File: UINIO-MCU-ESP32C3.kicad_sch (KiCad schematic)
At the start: 1 part

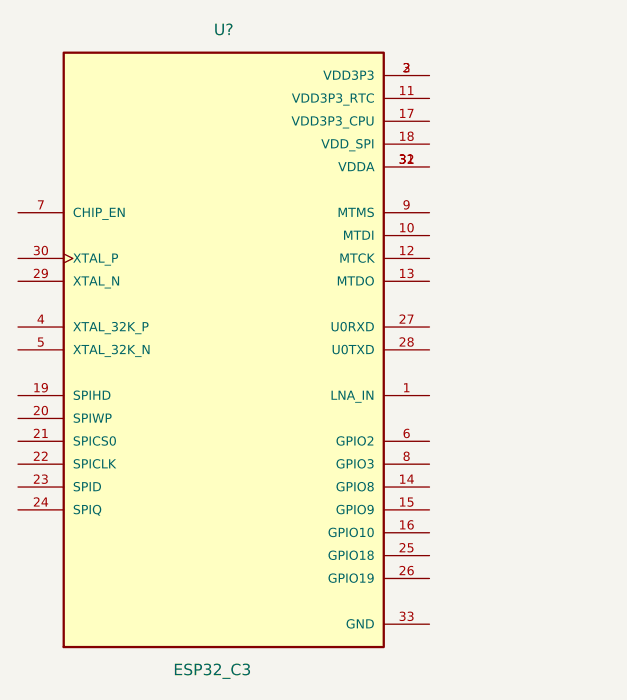
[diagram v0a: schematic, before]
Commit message: Replace ESP32-C3 Symbol.
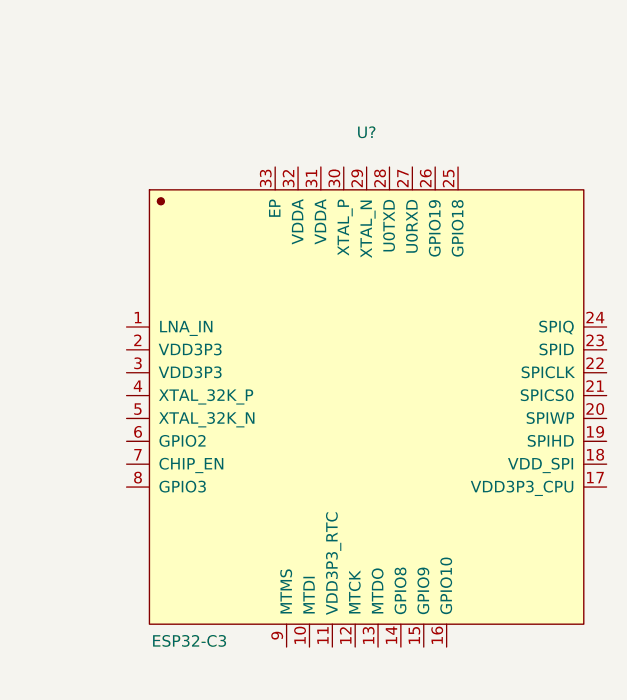
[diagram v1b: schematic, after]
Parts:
- removed U?: ESP32_C3, Uinio:QFN-32-5-5, symbol Uinio:ESP32_C3
- added U?: ESP32-C3, kicad_lceda:QFN-32_L5.0-W5.0-P0.50-TL-EP3.7, symbol Uinio:ESP32-C3
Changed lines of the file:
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@@
     (company "电子技术博客 UinIO.com")
   )
-  (symbol (lib_id "Uinio:ESP32_C3") (at 143.51 90.17 0) (unit 1)
+  (symbol (lib_id "Uinio:ESP32-C3") (at 154.305 96.52 0) (unit 1)
     (in_bom yes) (on_board yes)
-    (property "Reference" "U?" (id 0) (at 143.51 54.61 0))
-    (property "Value" "ESP32_C3" (id 1) (at 142.24 125.73 0))
-    (property "Footprint" "Uinio:QFN-32-5-5" (id 2) (at 132.08 127 0)
-      (effects (font (size 1.27 1.27)) (justify left bottom) hide)
+    (property "Reference" "U?" (id 0) (at 159.385 66.04 0))
+    (property "Value" "ESP32-C3" (id 1) (at 139.7 122.555 0))
+    (property "Footprint" "kicad_lceda:QFN-32_L5.0-W5.0-P0.50-TL-EP3.7" (id 2) (at 159.385 134.62 0)
+      (effects (font (size 1.27 1.27)) hide)
     )
-    (property "Datasheet" "" (id 3) (at 143.51 90.17 0)
-      (effects (font (size 1.27 1.27)) (justify left bottom) hide)
+    (property "Datasheet" "" (id 3) (at 154.305 76.8604 0)
+      (effects (font (size 1.27 1.27)) hide)
     )
-    (property "STANDARD" "" (id 4) (at 166.37 52.07 0)
-      (effects (font (size 1.27 1.27)) (justify left bottom) hide)
+    (property "SuppliersPartNumber" "C2838500" (id 4) (at 154.305 81.9404 0)
+      (effects (font (size 1.27 1.27)) hide)
     )
-    (property "MANUFACTURER" "" (id 5) (at 139.7 52.07 0)
-      (effects (font (size 1.27 1.27)) (justify left bottom) hide)
-    )
-    (property "PARTREV" "" (id 6) (at 163.83 49.53 0)
-      (effects (font (size 1.27 1.27)) (justify left bottom) hide)
-    )
-    (property "MAXIMUM_PACKAGE_HEIGHT" "" (id 7) (at 156.21 49.53 0)
-      (effects (font (size 1.27 1.27)) (justify left bottom) hide)
+    (property "uuid" "std:eaf37c2b292749de92559c0e914f3f30" (id 5) (at 160.655 138.43 0)
+      (effects (font (size 1.27 1.27)) hide)
     )
     (pin "1")
@@
   )
   (symbol_instances
-    (path "/826bd899-525d-4541-8e56-7c1d58c325f6"
-      (reference "U?") (unit 1) (value "ESP32_C3") (footprint "Uinio:QFN-32-5-5")
+    (path "/6af47f04-0cf9-428d-a0f2-32519eb3eeb0"
+      (reference "U?") (unit 1) (value "ESP32-C3") (footprint "kicad_lceda:QFN-32_L5.0-W5.0-P0.50-TL-EP3.7")
     )
   )

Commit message: update
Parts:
- added AE?: Antenna, symbol Device:Antenna
- added C? (x7): 0.1uF, symbol Device:C
- added C? (x2): 0.1uF, Capacitor_SMD:C_0603_1608Metric, symbol Device:C
- added C?: 1uF, Capacitor_SMD:C_0603_1608Metric, symbol Device:C
- added C? (x2): 15pF, symbol Device:C
- added C? (x2): 1uF, Capacitor_SMD:C_0402_1005Metric, symbol Uinio:CAP_0402
- added C? (x2): 1uF, symbol Device:C
- added C?: 10nF, symbol Device:C
- added D? (x2): BLUE LED, LED_SMD:LED_0603_1608Metric, symbol Device:LED
- added D?: Green LED, LED_SMD:LED_0603_1608Metric, symbol Device:LED
- added F?: Polyfuse, Fuse:Fuse_1206_3216Metric, symbol Device:Polyfuse
- added J?: 外接串行下载接口, symbol Connector:Conn_01x04_Male
- added L?: L, symbol Device:L
- added R? (x3): 10K, symbol Device:R
- added R?: 0R, symbol Device:R
- added R? (x3): 2K, Resistor_SMD:R_0603_1608Metric, symbol Device:R
- added SW?: 下载按键, Uinio:KEY-SMD_4P-L4.2-W3.4-P2.15-LS4.7, symbol Uinio:Key_YTS_A016S_1
- added SW?: 复位按键, Uinio:KEY-SMD_4P-L4.2-W3.4-P2.15-LS4.7, symbol Uinio:Key_YTS_A016S_1
- added U?: W25Q128JVSSIQ, kicad_lceda:SOIC-8_L5.3-W5.3-P1.27-LS8.0-BL, symbol Uinio:W25Q128JVSSIQ
- added U?: CH343P, kicad_lceda:TQFN-16_L3.0-W3.0-P0.50-BL-EP1.7, symbol Uinio:CH343P
- added U?: ME6211C33M5G-N, Uinio:SOT-23-5_L3.0-W1.7-P0.95-LS2.8-BR, symbol Uinio:ME6211
- added USB?: USB_Type_C_16Pin, Uinio:USB-C-SMD_TYPEC-304J-BCP16, symbol Uinio:USB_Type_C_16Pin
- added VT? (x2): S8050, Uinio:SOT-23-3_L2.9-W1.6-P1.90-LS2.9-BL, symbol Uinio:S8050
- added Y?: Crystal_GND24, symbol Device:Crystal_GND24
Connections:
- net at U?.1 (LNA_IN): now also C?.1, L?.2
- net GPIO5/ADC2/SCL: now reaches U?.10 (MTDI)
- net SPIHD: now reaches U?.11 (VDD3P3_RTC)
- net SPIHD: now also U?.17 (VDD3P3_CPU), U?.2 (VDD3P3), U?.3 (VDD3P3), U?.31 (VDDA), U?.32 (VDDA), C?.1, C?.1, C?.1, C?.1, C?.1, C?.1, C?.1, C?.2, R?.2, U?.3 (WP#(IO2)), U?.5 (Vout), U?.7 (HOLD#/RESET#/(IO3)), U?.8 (VCC)
- net GPIO6: now reaches U?.12 (MTCK)
- net GPIO7: now reaches U?.13 (MTDO)
- net GPIO8/PWM: now reaches U?.14 (GPIO8)
- net GPIO9/BOOT: now reaches U?.15 (GPIO9)
- net GPIO9/BOOT: now also R?.1, SW?.3, SW?.4, VT?.3 (C)
- net GPIO10: now reaches U?.16 (GPIO10)
- net VDD_SPI/GPIO11: now reaches U?.18 (VDD_SPI)
- net VDD_SPI/GPIO11: now also C?.1
- net SPIHD/GPIO12: now reaches U?.19 (SPIHD)
- net SPIWP/GPIO13: now reaches U?.20 (SPIWP)
- net SPICS0: now reaches U?.21 (SPICS0)
- net SPICS0: now also U?.1 (CS#)
- net SPICLK: now reaches U?.22 (SPICLK)
- net SPICLK: now also U?.6 (CLK)
- net SPID: now reaches U?.23 (SPID)
- net SPID: now also U?.5 (DI(IO0))
- net SPIQ: now reaches U?.24 (SPIQ)
- net SPIQ: now also U?.2 (DO(IO1))
- net GPIO18/USB_D-: now reaches U?.25 (GPIO18)
- net GPIO19/USB_D+: now reaches U?.26 (GPIO19)
- net U0RXD: now reaches U?.27 (U0RXD)
- net U0RXD: now also J?.3 (Pin_3)
- net U0TXD: now reaches U?.28 (U0TXD)
- net U0TXD: now also J?.2 (Pin_2)
- net at U?.29 (XTAL_N): now also C?.2, Y?.3
- net at U?.30 (XTAL_P): now also R?.2
- net GND: now reaches U?.33 (EP)
- net GND: now also C?.1, C?.1, C?.1, C?.1, C?.1, C?.1, C?.2, C?.2, C?.2, C?.2, C?.2, C?.2, C?.2, C?.2, C?.2, C?.2, C?.2, D?.1 (K), SW?.1, SW?.1, SW?.2, SW?.2, U?.17 (EP), U?.2 (GND), U?.2 (Vss), U?.4 (GND), USB?.13 (GND), USB?.14 (GND), USB?.15 (GND), USB?.16 (GND), USB?.A1B12 (GND), USB?.B1A12 (GND), Y?.2, Y?.4
- net GPIO0/U1TXD: now reaches U?.4 (XTAL_32K_P)
- net GPIO1/U1RXD: now reaches U?.5 (XTAL_32K_N)
- net GPIO2: now reaches U?.6 (GPIO2)
- net CHIP_EN: now reaches U?.7 (CHIP_EN)
- net CHIP_EN: now also SW?.3, SW?.4, VT?.3 (C)
- net GPIO3: now reaches U?.8 (GPIO3)
- net GPIO4/ADC1/SDA: now reaches U?.9 (MTMS)
- new net: R?.2, VT?.1 (B) (x2)
- new net: C?.2, R?.1, Y?.1
- new net: AE?.1 (A), C?.1, L?.1
- new net: D?.1 (K), R?.2 (x2)
- new net: D?.2 (A), R?.1
- new net: F?.1, USB?.A4B9 (VBUS), USB?.B4A9 (VBUS)
- new net CH343_ACT#: U?.10 (ACT#)
- new net CH343_CTS: U?.15 (CTS)
- new net CH343_DCD: U?.11 (DCD)
- new net CH343_DSR: U?.14 (DSR)
- new net CH343_DTR: U?.12 (DTRTNOW)
- new net CH343_RI: U?.16 (RI)
- new net CH343_RTS: U?.13 (RTS)
- new net CH343_RXD: R?.1, U?.5 (RXD)
- new net CH343_TXD: R?.1, U?.4 (TXD)
- new net CH343_USB_Data_N: U?.8 (UD-), USB?.A7 (DN1), USB?.B7 (DN2)
- new net CH343_USB_Data_P: U?.7 (UD+), USB?.A6 (DP1), USB?.B6 (DP2)
- new net CH343_VDD_3.3V: C?.2, U?.6 (V3)
- new net CH343_VDD_5V: C?.2, F?.2, R?.2, U?.3 (VDD5), U?.9 (VBUS)
- new net CH343_VIO: C?.1, D?.2 (A), D?.2 (A), U?.1 (VIO)
- new net DTR: J?.1 (Pin_1), R?.1, VT?.2 (E)
- new net RTS: J?.4 (Pin_4), R?.1, VT?.2 (E)
- new net VDD_5V: C?.2, U?.1 (Vin), U?.3 (CE)
- no-connect marks 0 -> 5
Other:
- note added: "ME6211C33M5G-N 供电电路"
- moved on the sheet: U?

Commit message: update
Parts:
- removed D? (x2): BLUE LED, LED_SMD:LED_0603_1608Metric, symbol Device:LED
- removed R? (x2): 2K, Resistor_SMD:R_0603_1608Metric, symbol Device:R
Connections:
- net CH343_DTR is gone; now on net DTR: U?.12 (DTRTNOW)
- net CH343_RTS is gone; now on net RTS: U?.13 (RTS)
- net CH343_VDD_3.3V is gone; now on net SPIHD: C?.2, U?.6 (V3)
- net CH343_VIO is gone; now on net SPIHD: C?.1, U?.1 (VIO)
- net CH343_VDD_5V: no longer C?.2, U?.3 (VDD5), U?.9 (VBUS)
- net VDD_5V: now also C?.2, U?.3 (VDD5), U?.9 (VBUS)
- net CH343_ACT#: no longer names the net of U?.10 (ACT#)
- net CH343_CTS: no longer names the net of U?.15 (CTS)
- net CH343_DCD: no longer names the net of U?.11 (DCD)
- net CH343_DSR: no longer names the net of U?.14 (DSR)
- net CH343_RI: no longer names the net of U?.16 (RI)
- net CH343_RXD renamed RXD
- net CH343_TXD renamed TXD
- net CH343_USB_Data_N renamed USB_Data-
- net USB_Data-: no longer USB?.B7 (DN2)
- net CH343_USB_Data_P renamed USB_Data+
- net USB_Data+: no longer USB?.B6 (DP2)
- new net USB_Data_N: USB?.B7 (DN2)
- new net USB_Data_P: USB?.B6 (DP2)
- no-connect marks 5 -> 10
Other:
- moved on the sheet: AE?, C?, D?, F?, J?, L?, R?, SW?, U?, USB?, VT?, Y?

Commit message: update
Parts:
- added J? (x2): Conn_01x15_Male, symbol Connector:Conn_01x15_Male
- Y?: value Crystal_GND24 -> 40MHz
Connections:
- net CH343_VDD_5V is gone; now on net VDD_5V: F?.2, R?.2
- net CHIP_EN: now also J?.7 (Pin_7)
- net GND: now also J?.2 (Pin_2), J?.2 (Pin_2), J?.3 (Pin_3)
- net GPIO0/U1TXD: now also J?.4 (Pin_4)
- net GPIO10: now also J?.15 (Pin_15)
- net GPIO18/USB_D-: now also J?.8 (Pin_8)
- net GPIO19/USB_D+: now also J?.7 (Pin_7)
- net GPIO1/U1RXD: now also J?.5 (Pin_5)
- net GPIO2: now also J?.6 (Pin_6)
- net GPIO3: now also J?.8 (Pin_8)
- net GPIO4/ADC1/SDA: now also J?.10 (Pin_10)
- net GPIO5/ADC2/SCL: now also J?.9 (Pin_9)
- net GPIO6: now also J?.11 (Pin_11)
- net GPIO7: now also J?.12 (Pin_12)
- net GPIO8/PWM: now also J?.13 (Pin_13)
- net GPIO9/BOOT: now also J?.14 (Pin_14)
- net SPICLK: now also J?.11 (Pin_11)
- net SPICS0: now also J?.12 (Pin_12)
- net SPID: now also J?.10 (Pin_10)
- net SPIHD: now also J?.3 (Pin_3), J?.4 (Pin_4)
- net SPIHD/GPIO12: now also J?.14 (Pin_14)
- net SPIQ: now also J?.9 (Pin_9)
- net SPIWP/GPIO13: now also J?.13 (Pin_13)
- net U0RXD: now also J?.6 (Pin_6)
- net U0TXD: now also J?.5 (Pin_5)
- net VDD_5V: now also J?.1 (Pin_1), J?.1 (Pin_1)
- net VDD_SPI/GPIO11: now also J?.15 (Pin_15)
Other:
- note added: "电源"
- note removed: "ME6211C33M5G-N 供电电路"
- moved on the sheet: AE?, C?, D?, F?, J?, L?, R?, SW?, U?, USB?, VT?, Y?

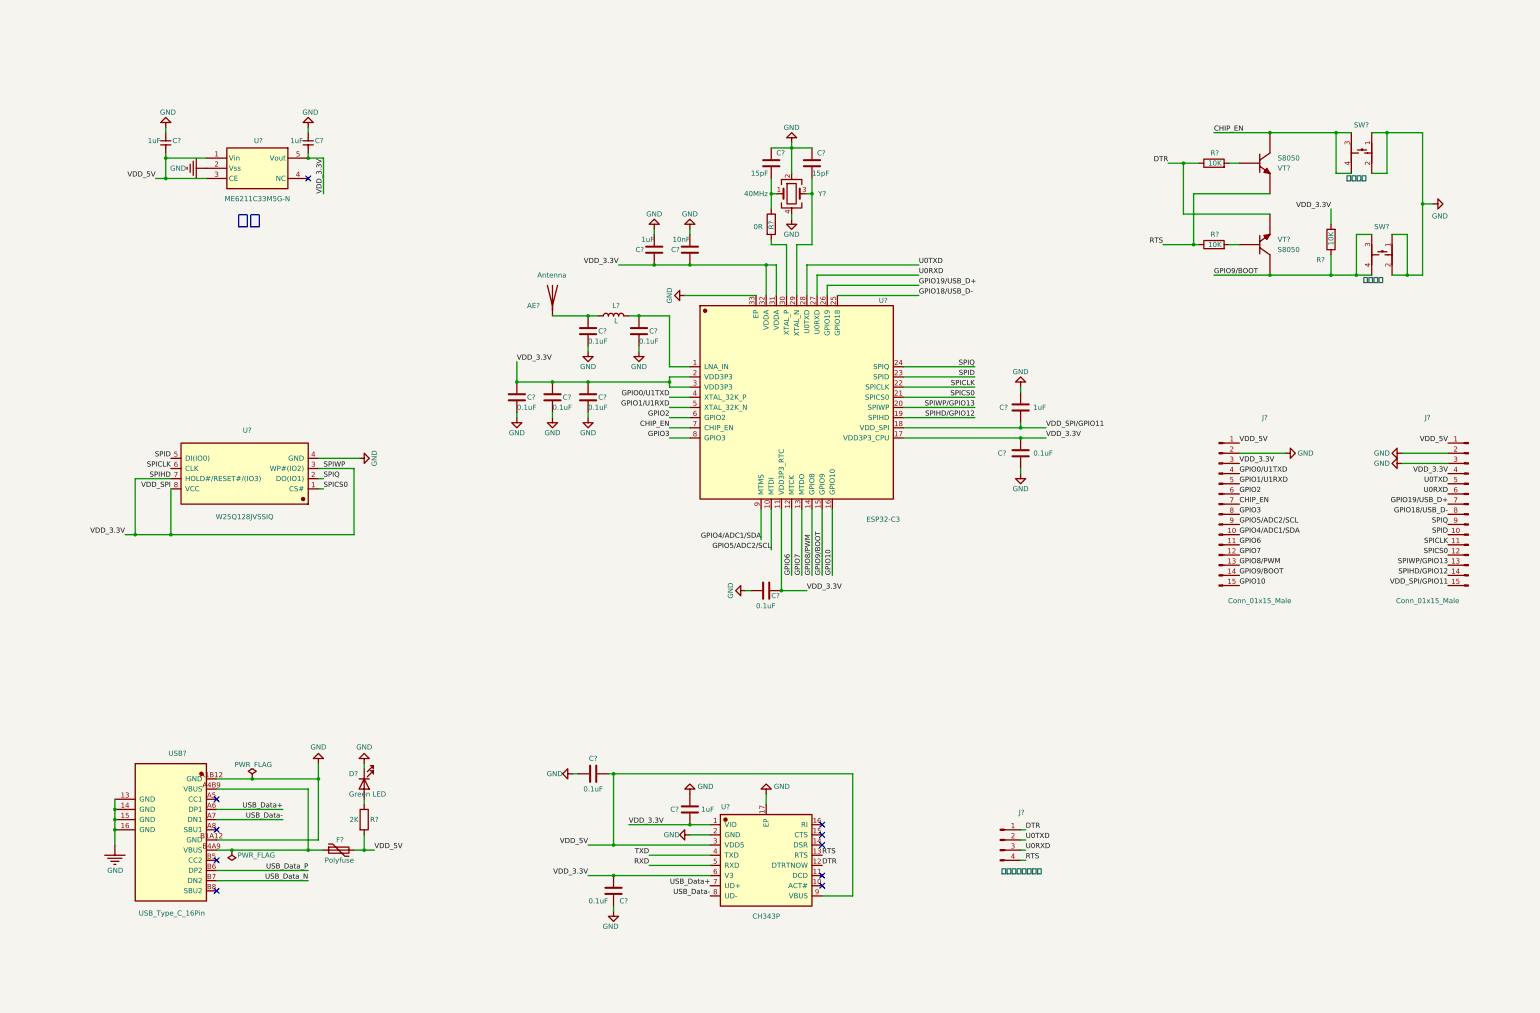
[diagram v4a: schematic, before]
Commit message: The schematic diagram is drawn.
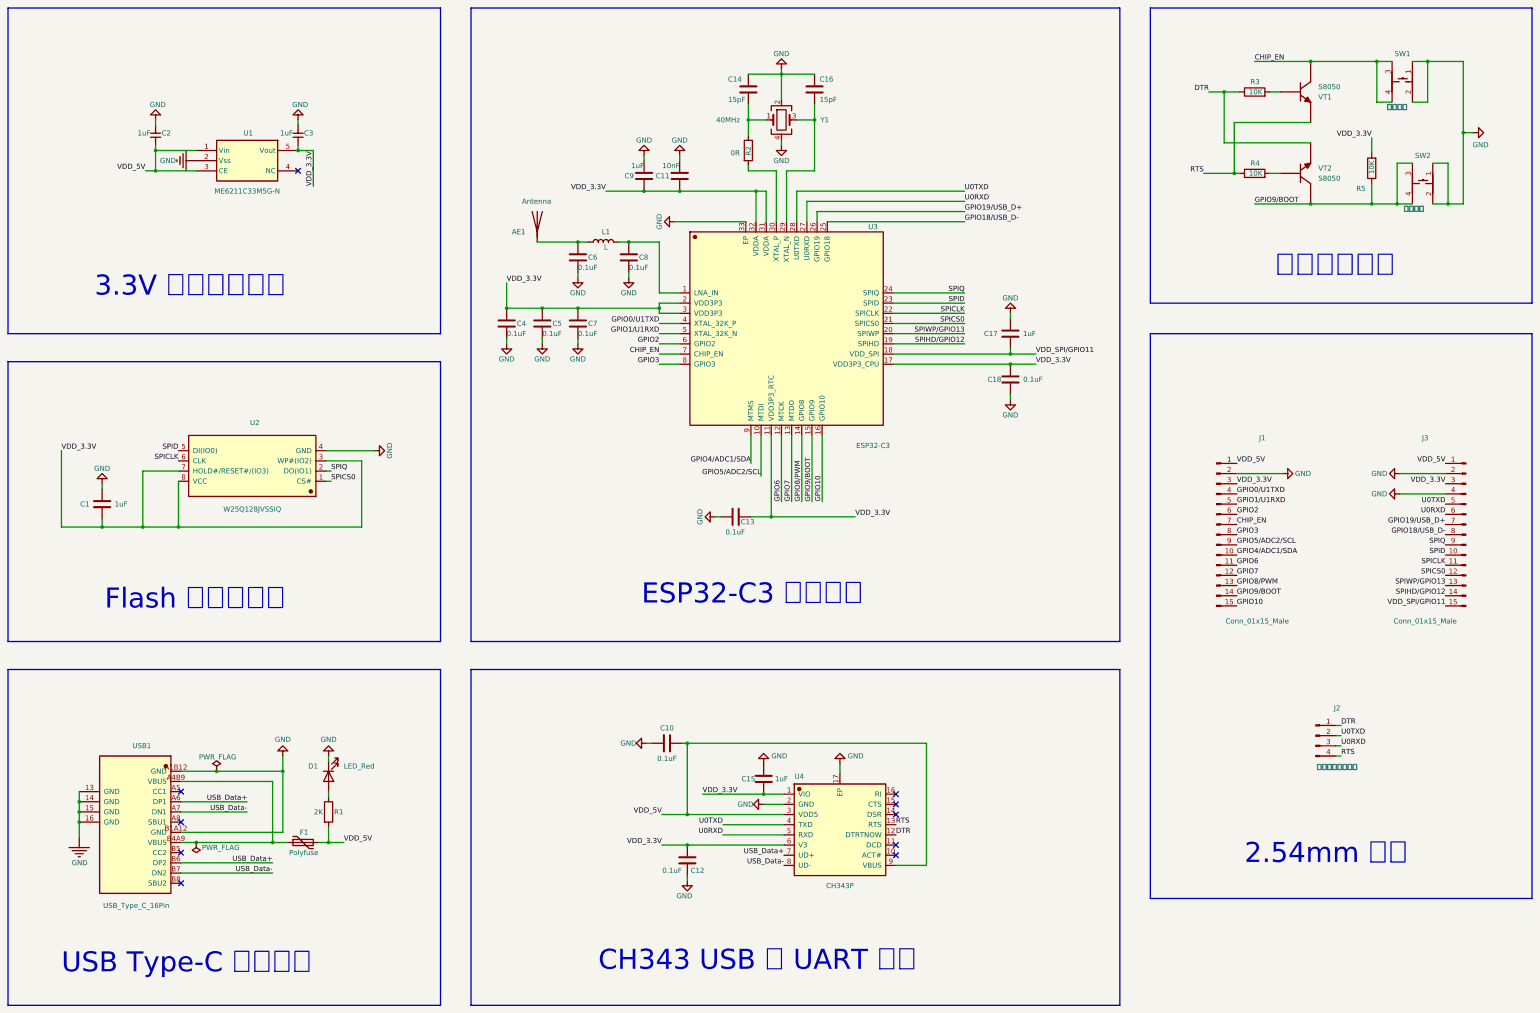
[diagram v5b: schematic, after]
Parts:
- added C1: 1uF, symbol Device:C
- D1: renamed from D?; value Green LED -> LED_Red
- gave numbers to parts that had none: 38
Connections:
- net RXD is gone; now on net U0RXD: U4.5 (RXD)
- net TXD is gone; now on net U0TXD: U4.4 (TXD)
- net USB_Data_N is gone; now on net USB_Data-: USB1.B7 (DN2)
- net USB_Data_P is gone; now on net USB_Data+: USB1.B6 (DP2)
- net GND: now also J3.4 (Pin_4), C1.2; no longer J3.3 (Pin_3)
- net SPIHD renamed VDD_3.3V
- net VDD_3.3V: now also J3.3 (Pin_3), C1.1; no longer J3.4 (Pin_4)
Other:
- note added: "2.54mm 排针"
- note added: "3.3V 线性稳压电路"
- note added: "CH343 USB 转 UART 电路"
- note added: "ESP32-C3 最小系统"
- note added: "Flash 存储器电路"
- note added: "USB Type-C 接口电路"
- note added: "下载控制电路"
- note removed: "电源"
- moved on the sheet: AE1, C10, C11, C12, C13, C14, C15, C16, C17, C18, C2, C3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
